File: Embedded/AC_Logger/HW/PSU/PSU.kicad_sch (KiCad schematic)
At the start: 11 parts, among them U1 L7809, U2 L7909

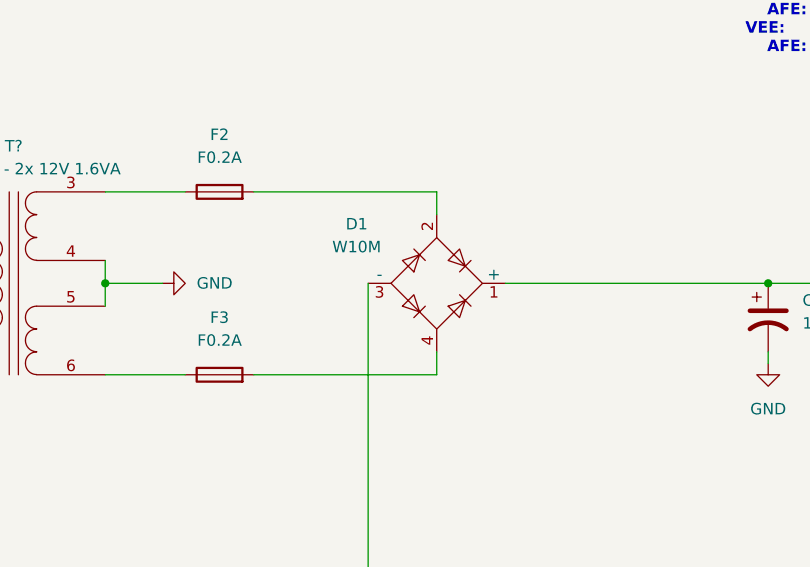
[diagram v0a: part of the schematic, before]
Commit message: PCB changed to make sandwitch.
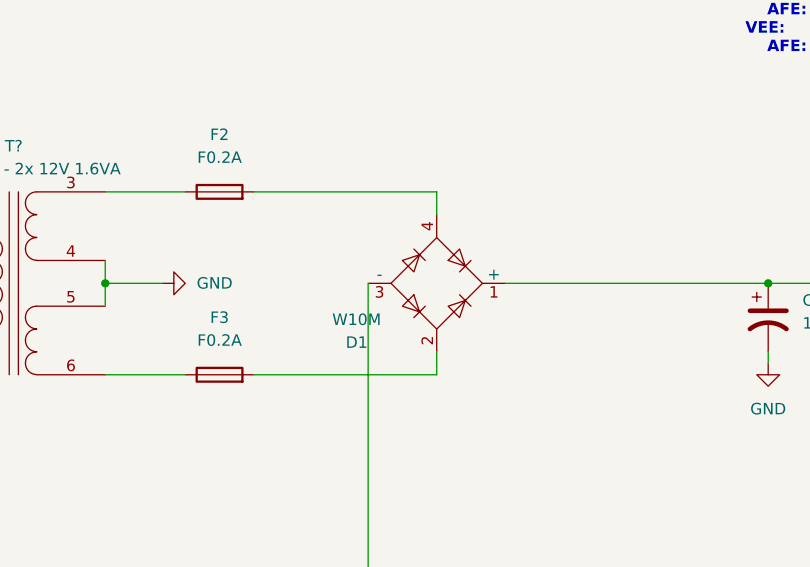
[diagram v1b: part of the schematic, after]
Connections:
- net at F3.2: now also D1.2; no longer D1.4
- net at F2.2: now also D1.4; no longer D1.2
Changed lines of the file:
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@@
 		(shape input)
 		(at 68.58 66.04 180)
-		(fields_autoplaced yes)
 		(effects
 			(font
@@
 		(shape input)
 		(at 52.07 55.88 180)
-		(fields_autoplaced yes)
 		(effects
 			(font
@@
 				)
 			)
+			(project ""
+				(path "/496f50f6-b2f3-4b8a-9f23-d0b8419323e8/259bb928-7a55-4782-aba9-7b00086dca40"
+					(reference "F3")
+					(unit 1)
+				)
+			)
 		)
 	)
@@
 				)
 			)
+			(project ""
+				(path "/496f50f6-b2f3-4b8a-9f23-d0b8419323e8/259bb928-7a55-4782-aba9-7b00086dca40"
+					(reference "#PWR05")
+					(unit 1)
+				)
+			)
 		)
 	)
@@
 				)
 			)
+			(project ""
+				(path "/496f50f6-b2f3-4b8a-9f23-d0b8419323e8/259bb928-7a55-4782-aba9-7b00086dca40"
+					(reference "#PWR08")
+					(unit 1)
+				)
+			)
 		)
 	)
@@
 		(lib_id "Diode_Bridge:W10G")
 		(at 132.08 60.96 0)
-		(mirror x)
-		(unit 1)
-		(exclude_from_sim no)
-		(in_bom yes)
-		(on_board yes)
-		(dnp no)
-		(fields_autoplaced yes)
+		(unit 1)
+		(exclude_from_sim no)
+		(in_bom yes)
+		(on_board yes)
+		(dnp no)
 		(property "Reference" "D1"
-			(at 123.19 54.3812 0)
+			(at 123.19 67.5388 0)
 			(effects
 				(font
@@
 		)
 		(property "Value" "W10M"
-			(at 123.19 56.9212 0)
+			(at 123.19 64.9988 0)
 			(effects
 				(font
@@
 		)
 		(property "Footprint" "Diode_THT:Diode_Bridge_Round_D9.8mm"
-			(at 135.89 64.135 0)
+			(at 135.89 57.785 0)
 			(effects
 				(font
@@
 			(project ""
 				(path "/09c92b2a-ba10-45d0-ac91-8ea09cf68577/7e974cae-0cca-453a-ab68-43db80964abd"
+					(reference "D1")
+					(unit 1)
+				)
+			)
+			(project ""
+				(path "/496f50f6-b2f3-4b8a-9f23-d0b8419323e8/259bb928-7a55-4782-aba9-7b00086dca40"
 					(reference "D1")
 					(unit 1)
@@
 				)
 			)
+			(project ""
+				(path "/496f50f6-b2f3-4b8a-9f23-d0b8419323e8/259bb928-7a55-4782-aba9-7b00086dca40"
+					(reference "#PWR012")
+					(unit 1)
+				)
+			)
 		)
 	)
@@
 				)
 			)
+			(project ""
+				(path "/496f50f6-b2f3-4b8a-9f23-d0b8419323e8/259bb928-7a55-4782-aba9-7b00086dca40"
+					(reference "U2")
+					(unit 1)
+				)
+			)
 		)
 	)
@@
 				)
 			)
+			(project ""
+				(path "/496f50f6-b2f3-4b8a-9f23-d0b8419323e8/259bb928-7a55-4782-aba9-7b00086dca40"
+					(reference "C3")
+					(unit 1)
+				)
+			)
 		)
 	)
@@
 				)
 			)
+			(project ""
+				(path "/496f50f6-b2f3-4b8a-9f23-d0b8419323e8/259bb928-7a55-4782-aba9-7b00086dca40"
+					(reference "T1")
+					(unit 1)
+				)
+			)
 		)
 	)
@@
 				)
 			)
+			(project ""
+				(path "/496f50f6-b2f3-4b8a-9f23-d0b8419323e8/259bb928-7a55-4782-aba9-7b00086dca40"
+					(reference "F2")
+					(unit 1)
+				)
+			)
 		)
 	)
@@
 			(project ""
 				(path "/09c92b2a-ba10-45d0-ac91-8ea09cf68577/7e974cae-0cca-453a-ab68-43db80964abd"
+					(reference "C4")
+					(unit 1)
+				)
+			)
+			(project ""
+				(path "/496f50f6-b2f3-4b8a-9f23-d0b8419323e8/259bb928-7a55-4782-aba9-7b00086dca40"
 					(reference "C4")
 					(unit 1)
@@
 				)
 			)
+			(project ""
+				(path "/496f50f6-b2f3-4b8a-9f23-d0b8419323e8/259bb928-7a55-4782-aba9-7b00086dca40"
+					(reference "#PWR04")
+					(unit 1)
+				)
+			)
 		)
 	)
@@
 				)
 			)
+			(project ""
+				(path "/496f50f6-b2f3-4b8a-9f23-d0b8419323e8/259bb928-7a55-4782-aba9-7b00086dca40"
+					(reference "#PWR09")
+					(unit 1)
+				)
+			)
 		)
 	)
@@
 				)
 			)
+			(project ""
+				(path "/496f50f6-b2f3-4b8a-9f23-d0b8419323e8/259bb928-7a55-4782-aba9-7b00086dca40"
+					(reference "#PWR06")
+					(unit 1)
+				)
+			)
 		)
 	)
@@
 				)
 			)
+			(project ""
+				(path "/496f50f6-b2f3-4b8a-9f23-d0b8419323e8/259bb928-7a55-4782-aba9-7b00086dca40"
+					(reference "#PWR010")
+					(unit 1)
+				)
+			)
 		)
 	)
@@
 			(project ""
 				(path "/09c92b2a-ba10-45d0-ac91-8ea09cf68577/7e974cae-0cca-453a-ab68-43db80964abd"
+					(reference "C1")
+					(unit 1)
+				)
+			)
+			(project ""
+				(path "/496f50f6-b2f3-4b8a-9f23-d0b8419323e8/259bb928-7a55-4782-aba9-7b00086dca40"
 					(reference "C1")
 					(unit 1)
@@
 				)
 			)
+			(project ""
+				(path "/496f50f6-b2f3-4b8a-9f23-d0b8419323e8/259bb928-7a55-4782-aba9-7b00086dca40"
+					(reference "#PWR011")
+					(unit 1)
+				)
+			)
 		)
 	)
@@
 				)
 			)
+			(project ""
+				(path "/496f50f6-b2f3-4b8a-9f23-d0b8419323e8/259bb928-7a55-4782-aba9-7b00086dca40"
+					(reference "#PWR07")
+					(unit 1)
+				)
+			)
 		)
 	)
@@
 				)
 			)
+			(project ""
+				(path "/496f50f6-b2f3-4b8a-9f23-d0b8419323e8/259bb928-7a55-4782-aba9-7b00086dca40"
+					(reference "U1")
+					(unit 1)
+				)
+			)
 		)
 	)
@@
 				)
 			)
+			(project ""
+				(path "/496f50f6-b2f3-4b8a-9f23-d0b8419323e8/259bb928-7a55-4782-aba9-7b00086dca40"
+					(reference "F1")
+					(unit 1)
+				)
+			)
 		)
 	)
@@
 					(reference "C2")
 					(unit 1)
+				)
+			)
+			(project ""
+				(path "/496f50f6-b2f3-4b8a-9f23-d0b8419323e8/259bb928-7a55-4782-aba9-7b00086dca40"
+					(reference "C2")
+					(unit 1)

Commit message: Corrections.
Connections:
- net GND: now also C2.1; no longer C2.2
- net at D1.3 (-), U2.2 (VI): now also C2.2; no longer C2.1
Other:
- moved on the sheet: C2
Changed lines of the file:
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@@
+	)
+	(junction
+		(at 168.91 96.52)
+		(diameter 0)
+		(color 0 0 0 0)
 	)
 	(junction
@@
 		(color 0 0 0 0)
 	)
-	(junction
-		(at 168.91 96.52)
-		(diameter 0)
-		(color 0 0 0 0)
-	)
 	(wire
 		(pts
@@
 	(wire
 		(pts
+			(xy 168.91 96.52) (xy 189.23 96.52)
+		)
+		(stroke
+			(width 0)
+			(type default)
+		)
+	)
+	(wire
+		(pts
 			(xy 111.76 50.8) (xy 132.08 50.8)
 		)
@@
 		(pts
 			(xy 168.91 69.85) (xy 168.91 68.58)
-		)
-		(stroke
-			(width 0)
-			(type default)
-		)
-	)
-	(wire
-		(pts
-			(xy 168.91 96.52) (xy 189.23 96.52)
 		)
 		(stroke
@@
 	(symbol
 		(lib_id "Device:C_Polarized_US")
-		(at 168.91 100.33 0)
+		(at 168.91 100.33 180)
 		(unit 1)
 		(exclude_from_sim no)
@@
 		(fields_autoplaced yes)
 		(property "Reference" "C2"
-			(at 172.72 98.4249 0)
-			(effects
-				(font
-					(size 1.27 1.27)
-				)
-				(justify left)
+			(at 172.72 99.6949 0)
+			(effects
+				(font
+					(size 1.27 1.27)
+				)
+				(justify right)
 			)
 		)
 		(property "Value" "1000u 16V"
-			(at 172.72 100.9649 0)
-			(effects
-				(font
-					(size 1.27 1.27)
-				)
-				(justify left)
-			)
-		)
+			(at 172.72 102.2349 0)
+			(effects
+				(font
+					(size 1.27 1.27)
+				)
+				(justify right)
+			)
+		)
